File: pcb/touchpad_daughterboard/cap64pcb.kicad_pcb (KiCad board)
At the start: 2 copper layers, 91.6 x 12 mm, 33 parts, among them J1 SM04B_SURS_TF, Q1 BSS138, Q2 BSS138, U1 MPR121QR2, U2 SPX3819-3.3

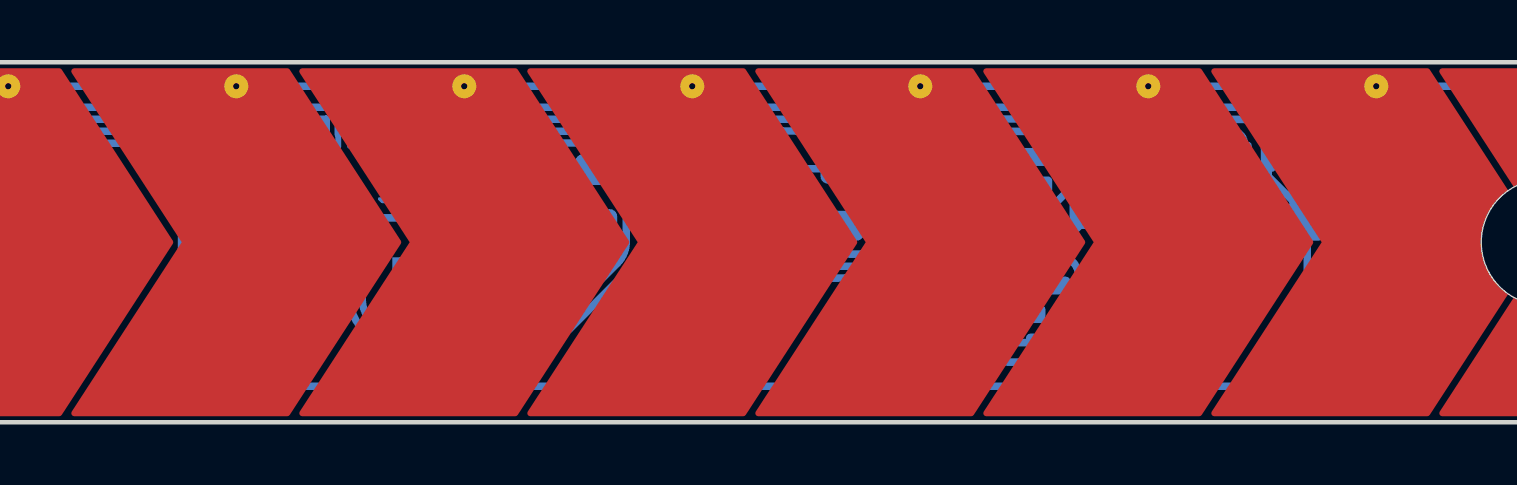
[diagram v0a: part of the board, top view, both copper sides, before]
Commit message: 5pin jst sur
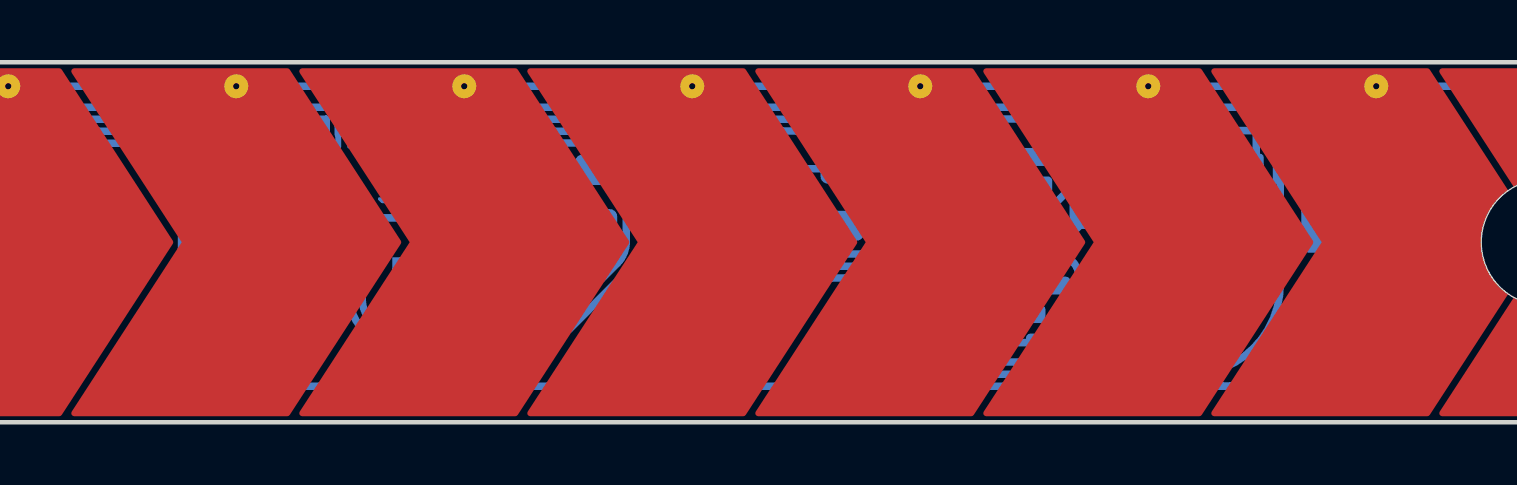
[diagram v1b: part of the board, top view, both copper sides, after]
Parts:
- H1, H2: value MountingHole -> MagnetHole
- J1: footprint Connector_JST:JST_SUR_SM04B-SURS-TF_1x04-1MP_P0.80mm_Horizontal -> Connector_JST:JST_SUR_SM05B-SURS-TF_1x05-1MP_P0.80mm_Horizontal
- moved J1 0.40 mm to (109.4, 43.7)
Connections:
- J1 pad 1: GND -> VIB
- J1 pad 3: Net-(J1-Pad3) -> GND
- Q1 pad 3: Net-(J1-Pad3) -> Net-(J1-Pad4)
- Q2 pad 3: Net-(J1-Pad4) -> Net-(Q2-Pad3)
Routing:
- net VIB: track 0.00 -> 20.6 mm
- net Net-(J1-Pad3): track 18.6 -> 0.00 mm
- net Net-(J1-Pad4): track 7.37 -> 17.8 mm
- net GND: track 82.9 -> 73.8 mm
- net Net-(Q2-Pad3): track 0.00 -> 6.57 mm
- net VCC: track 11.0 -> 12.1 mm

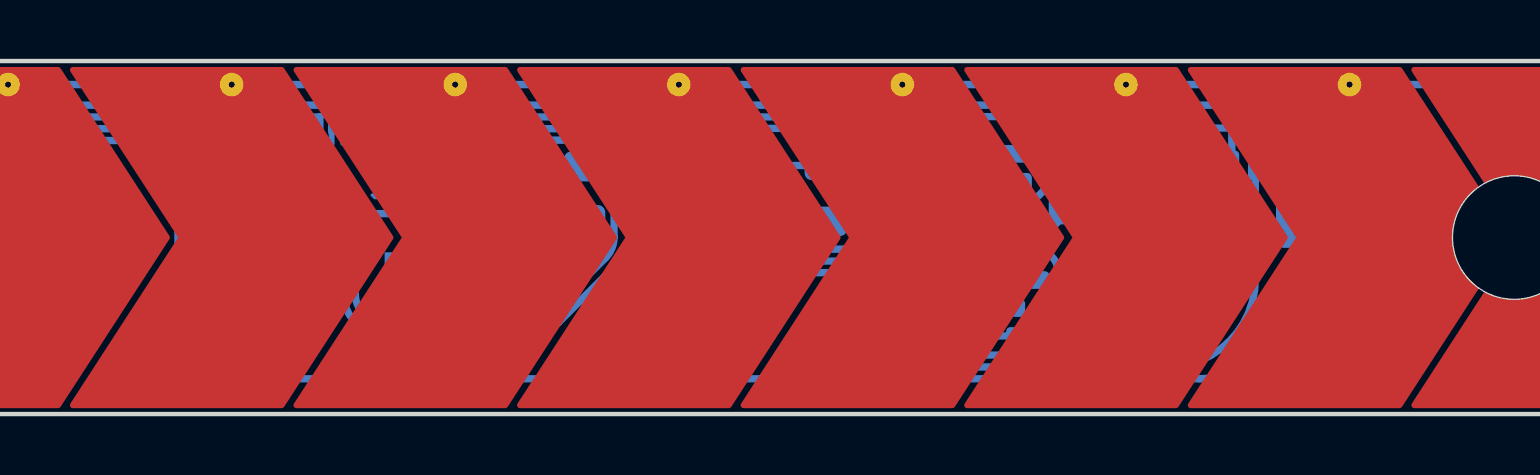
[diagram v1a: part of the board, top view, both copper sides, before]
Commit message: reorder and reroute connector
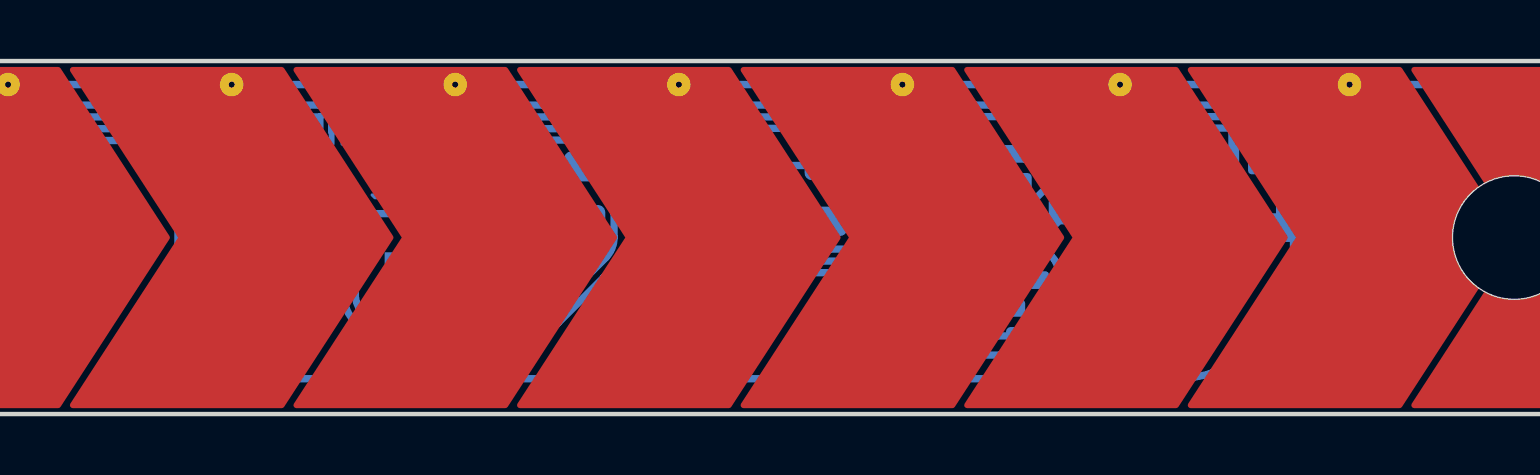
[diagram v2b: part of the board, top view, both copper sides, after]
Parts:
- moved J1 0.20 mm to (109.4, 43.5)
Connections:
- J1 pad 1: VIB -> VCC
- J1 pad 2: VCC -> GND
- J1 pad 3: GND -> VIB
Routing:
- net VIB: track 20.6 -> 5.75 mm
- net GND: track 73.8 -> 78.2 mm
- net VCC: track 12.1 -> 13.2 mm

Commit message: mcp moved
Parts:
- moved TP14 7.67 mm to (84.0, 54.0)
- moved TP13 7.60 mm to (87.5, 53.8)
- moved R1 6.80 mm to (68.9, 42.9)
- moved C5 6.80 mm to (68.9, 45.0)
- moved U1 6.70 mm to (73.3, 42.8)
- moved JP1 3.96 mm to (73.3, 46.7)
- moved D1 1.03 mm to (86.3, 43.7), turned to -90 degrees
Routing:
- net Net-(D1-Pad1): track 3.82 -> 12.7 mm
- net Net-(TP4-Pad1): track 19.2 -> 12.2 mm
- net Net-(TP7-Pad1): track 4.54 -> 11.3 mm
- net Net-(TP12-Pad1): track 41.8 -> 48.5 mm
- net Net-(TP9-Pad1): track 18.5 -> 25.2 mm
- net Net-(TP10-Pad1): track 26.1 -> 32.8 mm
- net Net-(TP2-Pad1): track 33.9 -> 27.2 mm
- net Net-(TP1-Pad1): track 41.7 -> 35.0 mm
- net Net-(TP3-Pad1): track 26.1 -> 19.4 mm
- net Net-(TP11-Pad1): track 34.1 -> 40.8 mm
- net Net-(TP8-Pad1): track 11.6 -> 18.0 mm
- net Net-(TP5-Pad1): track 12.0 -> 5.91 mm
- net SDA: track 27.6 -> 33.5 mm
- net GND: track 78.2 -> 83.4 mm
- net SCL: track 31.2 -> 35.3 mm
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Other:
- board text added: "Vibin'"

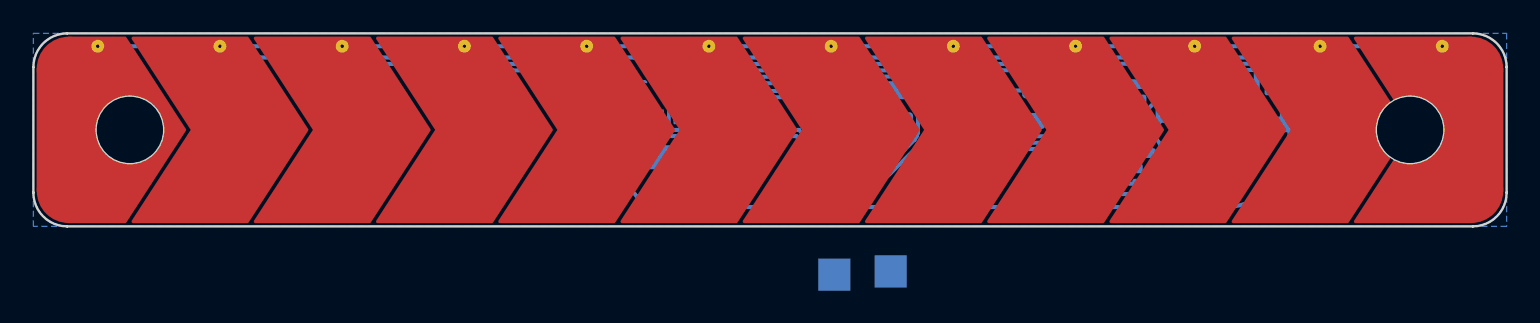
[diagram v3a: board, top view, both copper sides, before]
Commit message: space made for coin motor
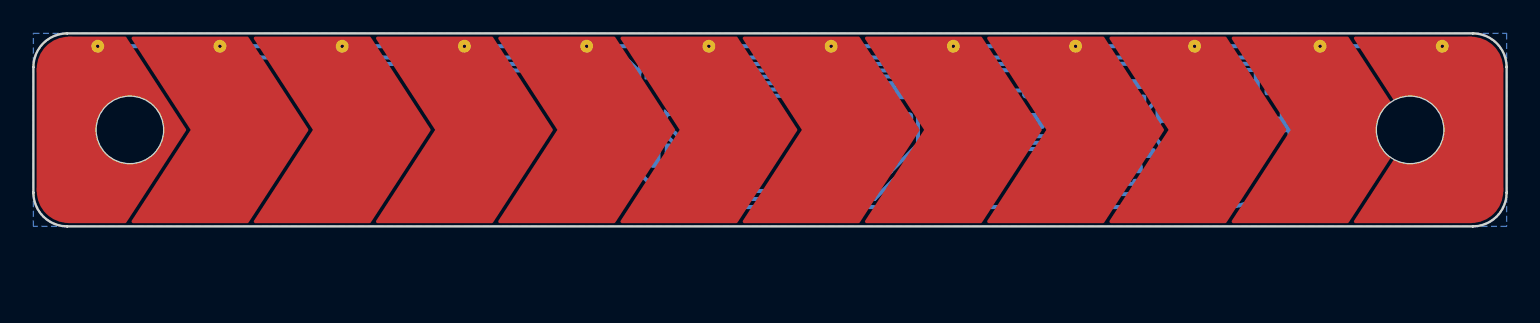
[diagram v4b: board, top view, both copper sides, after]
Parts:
- TP13, TP14: footprint TestPoint:TestPoint_Pad_2.0x2.0mm -> TestPoint:TestPoint_Pad_D1.0mm
- moved TP13 7.75 mm to (86.0, 46.2)
- moved TP14 6.04 mm to (85.3, 48.1)
- moved R1 0.67 mm to (68.6, 43.5)
- moved JP1 0.61 mm to (72.7, 46.6)
- moved U1 0.60 mm to (72.7, 42.8)
- moved C5 0.58 mm to (68.6, 45.5)
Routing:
- net +3V3: track 46.4 -> 52.9 mm
- net SCL: track 35.3 -> 37.7 mm
- net Net-(TP5-Pad1): track 5.91 -> 4.84 mm
- net GND: track 83.4 -> 82.7 mm
- net Net-(D1-Pad1): track 12.7 -> 13.4 mm
- net Net-(TP11-Pad1): track 40.8 -> 41.4 mm
- net Net-(TP1-Pad1): track 35.0 -> 34.4 mm
- net Net-(TP4-Pad1): track 12.2 -> 11.6 mm
- net Net-(TP9-Pad1): track 25.2 -> 25.8 mm
- net Net-(TP8-Pad1): track 18.0 -> 18.6 mm
- net Net-(TP3-Pad1): track 19.4 -> 18.8 mm
- net Net-(TP2-Pad1): track 27.2 -> 26.6 mm
- net Net-(TP12-Pad1): track 48.5 -> 49.1 mm
- net Net-(TP10-Pad1): track 32.8 -> 33.4 mm
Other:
- board text added: "0x5[abcd]"
- board text added: "vib"
- board text removed: "0x5"
- board text removed: "["
- board text removed: "]"
- board text removed: "abcd"

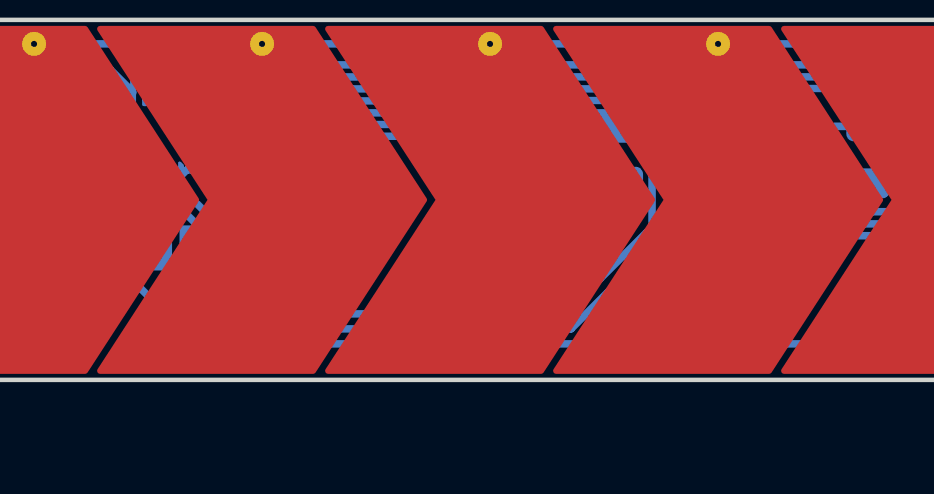
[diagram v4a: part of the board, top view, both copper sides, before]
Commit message: ERM symbol/footprint/3d model
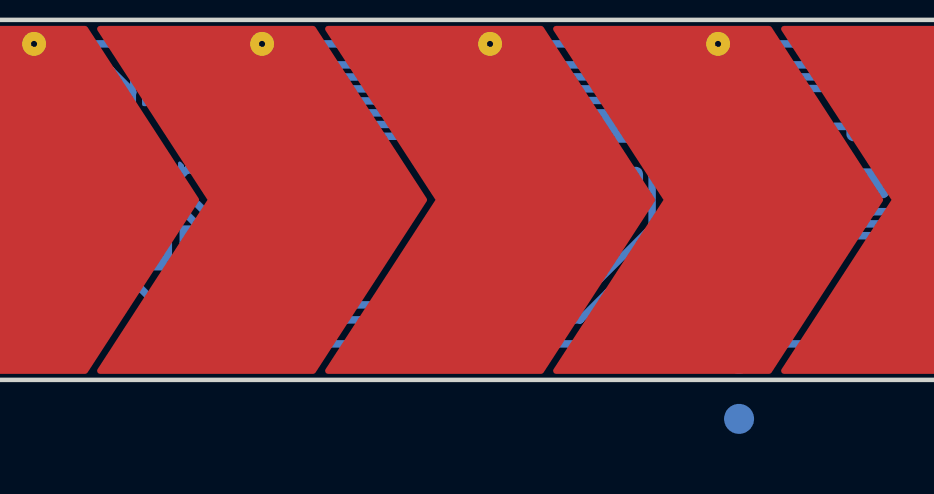
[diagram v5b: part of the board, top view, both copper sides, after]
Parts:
- added M1: Coin_Motor, coinERM:VC1018B001L, B.Cu at (80.0, 45.0)
- added TP15: +, TestPoint:TestPoint_Pad_D1.0mm, B.Cu at (92.1, 50.3)
- added TP16: -, TestPoint:TestPoint_Pad_D1.0mm, B.Cu at (92.1, 52.3)
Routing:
- net SCL: track 37.7 -> 36.8 mm

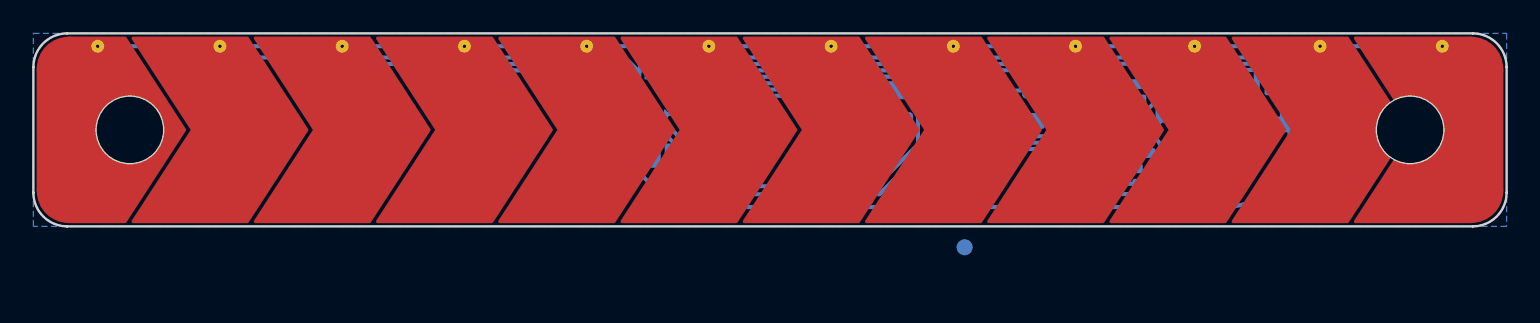
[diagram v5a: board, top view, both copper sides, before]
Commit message: erm footprint update, all routed, no errors
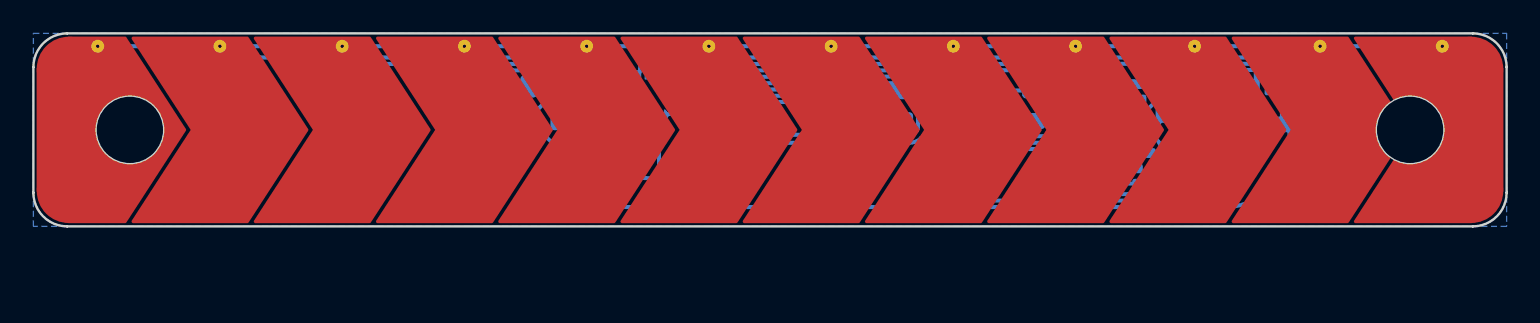
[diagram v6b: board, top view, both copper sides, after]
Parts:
- removed G***: LOGO, logo:bd_12mm
- TP15, TP16: footprint TestPoint:TestPoint_Pad_D1.0mm -> TestPoint:TestPoint_Pad_1.0x1.0mm
- moved TP14 13.3 mm to (72.1, 46.5)
- moved TP13 11.9 mm to (74.1, 46.5)
- moved TP15 3.94 mm to (90.3, 46.8)
- moved TP16 3.94 mm to (90.3, 48.8)
- moved JP1 3.80 mm to (68.9, 46.5)
- moved C5 2.95 mm to (65.9, 44.3)
- moved R1 2.95 mm to (65.9, 42.3)
- turned M1 to -20 degrees
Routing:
- net VIB: track 5.75 -> 25.3 mm
- net +3V3: track 52.9 -> 63.1 mm
- net GND: track 82.7 -> 88.8 mm
- net SDA: track 33.7 -> 37.4 mm
- net Net-(JP1-Pad2): track 2.58 -> 5.58 mm
- net Net-(R1-Pad1): track 1.92 -> 4.91 mm
- net Net-(C5-Pad1): track 2.89 -> 5.10 mm
- net SCL: track 36.8 -> 37.5 mm
